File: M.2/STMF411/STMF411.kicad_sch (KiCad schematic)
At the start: 23 parts, among them M1 M.2_Key_E, Q1 2N7002, U1 LDK120PU-R_DFN6, U2 STM32F411CCUx, Y1 16 MHz

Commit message: touchups to f411
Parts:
- added L1: TapTap Logo, LogoSmall:tt_4mm, symbol Mechanical:MountingHole
- added SW1: RESET, LogoSmall:LogoSmall, symbol Switch:SW_SPST
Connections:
- net +3V3: now also SW1.2 (B)
- net BOOT0: now also SW1.1 (A)
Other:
- note added: "Fancy Logos and shit"
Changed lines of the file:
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@@
     (stroke (width 0) (type solid) (color 0 0 0 0))
   )
-  (polyline (pts (xy 17.145 80.01) (xy 17.145 101.6))
+  (polyline (pts (xy 17.145 81.28) (xy 17.145 102.87))
     (stroke (width 0) (type solid) (color 0 0 0 0))
   )
@@
     (stroke (width 0) (type solid) (color 141 210 114 1))
   )
+  (polyline (pts (xy 17.145 118.11) (xy 100.33 118.11))
+    (stroke (width 0) (type solid) (color 0 0 0 0))
+  )
   (wire (pts (xy 38.735 29.21) (xy 46.355 29.21))
     (stroke (width 0) (type solid) (color 141 210 114 1))
@@
     (stroke (width 0) (type default) (color 0 0 0 0))
   )
+  (polyline (pts (xy 283.845 13.335) (xy 283.845 127.635))
+    (stroke (width 0) (type default) (color 0 0 0 0))
+  )
+  (wire (pts (xy 144.145 31.115) (xy 146.685 31.115))
+    (stroke (width 0) (type default) (color 0 0 0 0))
+  )
+  (wire (pts (xy 19.685 38.1) (xy 19.685 34.29))
+    (stroke (width 0) (type solid) (color 141 210 114 1))
+  )
+  (polyline (pts (xy 17.145 19.05) (xy 56.515 19.05))
+    (stroke (width 0) (type solid) (color 0 0 0 0))
+  )
+  (wire (pts (xy 108.585 29.21) (xy 108.585 31.75))
+    (stroke (width 0) (type default) (color 0 0 0 0))
+  )
+  (wire (pts (xy 106.68 53.975) (xy 106.68 52.705))
+    (stroke (width 0) (type solid) (color 141 210 114 1))
+  )
+  (wire (pts (xy 106.68 46.355) (xy 126.365 46.355))
+    (stroke (width 0) (type default) (color 0 0 0 0))
+  )
+  (polyline (pts (xy 95.25 19.05) (xy 182.245 19.05))
+    (stroke (width 0) (type solid) (color 0 0 0 0))
+  )
+  (wire (pts (xy 144.145 109.855) (xy 146.685 109.855))
+    (stroke (width 0) (type default) (color 0 0 0 0))
+  )
+  (wire (pts (xy 218.44 32.385) (xy 233.045 32.385))
+    (stroke (width 0) (type default) (color 0 0 0 0))
+  )
+  (wire (pts (xy 126.365 53.975) (xy 119.38 53.975))
+    (stroke (width 0) (type default) (color 0 0 0 0))
+  )
+  (wire (pts (xy 46.99 62.23) (xy 46.99 64.77))
+    (stroke (width 0) (type default) (color 0 0 0 0))
+  )
+  (wire (pts (xy 48.895 29.21) (xy 46.355 29.21))
+    (stroke (width 0) (type solid) (color 141 210 114 1))
+  )
+  (wire (pts (xy 141.605 109.855) (xy 144.145 109.855))
+    (stroke (width 0) (type default) (color 0 0 0 0))
+  )
+  (wire (pts (xy 275.59 29.845) (xy 260.985 29.845))
+    (stroke (width 0) (type default) (color 0 0 0 0))
+  )
+  (polyline (pts (xy 17.145 76.835) (xy 92.075 76.835))
+    (stroke (width 0) (type solid) (color 0 0 0 0))
+  )
+  (wire (pts (xy 40.64 62.23) (xy 40.64 66.04))
+    (stroke (width 0) (type default) (color 0 0 0 0))
+  )
+  (wire (pts (xy 139.065 109.855) (xy 141.605 109.855))
+    (stroke (width 0) (type default) (color 0 0 0 0))
+  )
+  (polyline (pts (xy 56.515 19.05) (xy 56.515 48.26))
+    (stroke (width 0) (type solid) (color 0 0 0 0))
+  )
+  (wire (pts (xy 90.17 88.9) (xy 80.01 88.9))
+    (stroke (width 0) (type solid) (color 141 210 114 1))
+  )
   (wire (pts (xy 19.685 24.13) (xy 46.355 24.13))
-    (stroke (width 0) (type solid) (color 141 210 114 1))
-  )
-  (polyline (pts (xy 283.845 13.335) (xy 283.845 127.635))
-    (stroke (width 0) (type default) (color 0 0 0 0))
-  )
-  (wire (pts (xy 144.145 31.115) (xy 146.685 31.115))
-    (stroke (width 0) (type default) (color 0 0 0 0))
-  )
-  (wire (pts (xy 19.685 38.1) (xy 19.685 34.29))
-    (stroke (width 0) (type solid) (color 141 210 114 1))
-  )
-  (polyline (pts (xy 17.145 19.05) (xy 56.515 19.05))
-    (stroke (width 0) (type solid) (color 0 0 0 0))
-  )
-  (wire (pts (xy 108.585 29.21) (xy 108.585 31.75))
-    (stroke (width 0) (type default) (color 0 0 0 0))
-  )
-  (wire (pts (xy 106.68 53.975) (xy 106.68 52.705))
-    (stroke (width 0) (type solid) (color 141 210 114 1))
-  )
-  (wire (pts (xy 106.68 46.355) (xy 126.365 46.355))
-    (stroke (width 0) (type default) (color 0 0 0 0))
-  )
-  (polyline (pts (xy 95.25 19.05) (xy 182.245 19.05))
-    (stroke (width 0) (type solid) (color 0 0 0 0))
-  )
-  (wire (pts (xy 144.145 109.855) (xy 146.685 109.855))
-    (stroke (width 0) (type default) (color 0 0 0 0))
-  )
-  (wire (pts (xy 218.44 32.385) (xy 233.045 32.385))
-    (stroke (width 0) (type default) (color 0 0 0 0))
-  )
-  (wire (pts (xy 126.365 53.975) (xy 119.38 53.975))
-    (stroke (width 0) (type default) (color 0 0 0 0))
-  )
-  (wire (pts (xy 46.99 62.23) (xy 46.99 64.77))
-    (stroke (width 0) (type default) (color 0 0 0 0))
-  )
-  (wire (pts (xy 48.895 29.21) (xy 46.355 29.21))
-    (stroke (width 0) (type solid) (color 141 210 114 1))
-  )
-  (wire (pts (xy 141.605 109.855) (xy 144.145 109.855))
-    (stroke (width 0) (type default) (color 0 0 0 0))
-  )
-  (wire (pts (xy 275.59 29.845) (xy 260.985 29.845))
-    (stroke (width 0) (type default) (color 0 0 0 0))
-  )
-  (polyline (pts (xy 17.145 76.835) (xy 92.075 76.835))
-    (stroke (width 0) (type solid) (color 0 0 0 0))
-  )
-  (wire (pts (xy 40.64 62.23) (xy 40.64 66.04))
-    (stroke (width 0) (type default) (color 0 0 0 0))
-  )
-  (wire (pts (xy 139.065 109.855) (xy 141.605 109.855))
-    (stroke (width 0) (type default) (color 0 0 0 0))
-  )
-  (polyline (pts (xy 56.515 19.05) (xy 56.515 48.26))
-    (stroke (width 0) (type solid) (color 0 0 0 0))
-  )
-  (wire (pts (xy 90.17 88.9) (xy 80.01 88.9))
     (stroke (width 0) (type solid) (color 141 210 114 1))
   )
@@
     (stroke (width 0) (type default) (color 0 0 0 0))
   )
+  (polyline (pts (xy 100.33 118.11) (xy 100.33 106.68))
+    (stroke (width 0) (type solid) (color 0 0 0 0))
+  )
   (wire (pts (xy 46.355 43.18) (xy 38.735 43.18))
     (stroke (width 0) (type solid) (color 141 210 114 1))
@@
     (stroke (width 0) (type solid) (color 0 0 0 0))
   )
+  (polyline (pts (xy 17.145 106.68) (xy 17.145 118.11))
+    (stroke (width 0) (type solid) (color 0 0 0 0))
+  )
   (wire (pts (xy 31.115 93.98) (xy 42.545 93.98))
     (stroke (width 0) (type solid) (color 141 210 114 1))
@@
   (polyline (pts (xy 283.845 13.335) (xy 186.055 13.335))
     (stroke (width 0) (type default) (color 0 0 0 0))
+  )
+  (polyline (pts (xy 100.33 106.68) (xy 17.145 106.68))
+    (stroke (width 0) (type solid) (color 0 0 0 0))
   )
   (polyline (pts (xy 186.055 13.335) (xy 13.335 13.335))
@@
     (effects (font (size 1.27 1.27)) (justify left bottom))
   )
+  (text "Fancy Logos and shit" (at 17.145 105.41 0)
+    (effects (font (size 1.27 1.27)) (justify left bottom))
+  )
   (text "Microcontroller Decoupling" (at 17.145 80.01 0)
     (effects (font (size 1.27 1.27)) (justify left bottom))
@@
     (property "Intersheet References" "${INTERSHEET_REFS}" (id 0) (at 120.2024 71.6756 0)
       (effects (font (size 1.27 1.27)) (justify right) hide)
+    )
+  )
+  (global_label "reset" (shape input) (at 54.61 112.395 0) (fields_autoplaced)
+    (effects (font (size 1.27 1.27)) (justify left))
+    (property "Intersheet References" "${INTERSHEET_REFS}" (id 0) (at 61.7402 112.4744 0)
+      (effects (font (size 1.27 1.27)) (justify left) hide)
     )
   )
@@
     (pin "1")
   )
+  (symbol (lib_id "Switch:SW_SPST") (at 49.53 112.395 0) (mirror y) (unit 1)
+    (in_bom yes) (on_board yes)
+    (property "Reference" "SW1" (id 0) (at 38.735 110.49 0))
+    (property "Value" "RESET" (id 1) (at 38.735 113.03 0))
+    (property "Footprint" "LogoSmall:LogoSmall" (id 2) (at 49.53 112.395 0)
+      (effects (font (size 1.27 1.27)) hide)
+    )
+    (property "Datasheet" "~" (id 3) (at 49.53 112.395 0)
+      (effects (font (size 1.27 1.27)) hide)
+    )
+    (pin "1")
+    (pin "2")
+  )
   (symbol (lib_id "power:+5V") (at 275.59 29.845 0) (unit 1)
     (in_bom yes) (on_board yes)
@@
     (pin "1")
   )
+  (symbol (lib_id "power:+3.3V") (at 44.45 112.395 0) (unit 1)
+    (in_bom yes) (on_board yes)
+    (property "Reference" "#PWR?" (id 0) (at 44.45 116.205 0)
+      (effects (font (size 1.27 1.27)) hide)
+    )
+    (property "Value" "+3.3V" (id 1) (at 48.26 109.855 0))
+    (property "Footprint" "" (id 2) (at 44.45 112.395 0)
+      (effects (font (size 1.27 1.27)) hide)
+    )
+    (property "Datasheet" "" (id 3) (at 44.45 112.395 0)
+      (effects (font (size 1.27 1.27)) hide)
+    )
+    (pin "1")
+  )
   (symbol (lib_id "power:PWR_FLAG") (at 260.985 29.845 0) (unit 1)
     (in_bom yes) (on_board yes)
@@
     )
     (pin "1")
+  )
+  (symbol (lib_id "Mechanical:MountingHole") (at 71.755 111.76 0) (unit 1)
+    (in_bom yes) (on_board yes) (fields_autoplaced)
+    (property "Reference" "L1" (id 0) (at 74.93 110.4899 0)
+      (effects (font (size 1.27 1.27)) (justify left))
+    )
+    (property "Value" "TapTap Logo" (id 1) (at 74.93 113.0299 0)
+      (effects (font (size 1.27 1.27)) (justify left))
+    )
+    (property "Footprint" "LogoSmall:tt_4mm" (id 2) (at 71.755 111.76 0)
+      (effects (font (size 1.27 1.27)) hide)
+    )
+    (property "Datasheet" "~" (id 3) (at 71.755 111.76 0)
+      (effects (font (size 1.27 1.27)) hide)
+    )
   )
   (symbol (lib_id "power:GND") (at 106.68 53.975 0) (unit 1)
@@
       (reference "#PWR0122") (unit 1) (value "+3.3V") (footprint "")
     )
+    (path "/ad402068-7356-4a93-a5af-216a06e3804c"
+      (reference "#PWR?") (unit 1) (value "+3.3V") (footprint "")
+    )
     (path "/42ec88f7-d7f3-40cf-8759-f8c5477df41e"
       (reference "C1") (unit 1) (value "4.7uF") (footprint "Capacitor_SMD:C_0402_1005Metric")
@@
       (reference "H1") (unit 1) (value "MountingHole_Pad") (footprint "MountingHole:MountingHole_3.2mm_M3_Pad_Via")
     )
+    (path "/c6faf540-b2b4-4eb8-b3ae-c8820f05ccf2"
+      (reference "L1") (unit 1) (value "TapTap Logo") (footprint "LogoSmall:tt_4mm")
+    )
     (path "/09ab82c3-34e9-44f6-bcc6-a88b0ac9235b"
       (reference "M1") (unit 1) (value "M.2_Key_E") (footprint "m2ngff:m2-padKeyE")
@@
       (reference "R5") (unit 1) (value "100k") (footprint "Resistor_SMD:R_0402_1005Metric")
     )
+    (path "/7cf0f891-8a1a-40d2-a263-a0d273d44d57"
+      (reference "SW1") (unit 1) (value "RESET") (footprint "LogoSmall:LogoSmall")
+    )
     (path "/91a43a45-d59b-41ce-8612-b88cf8bbc380"

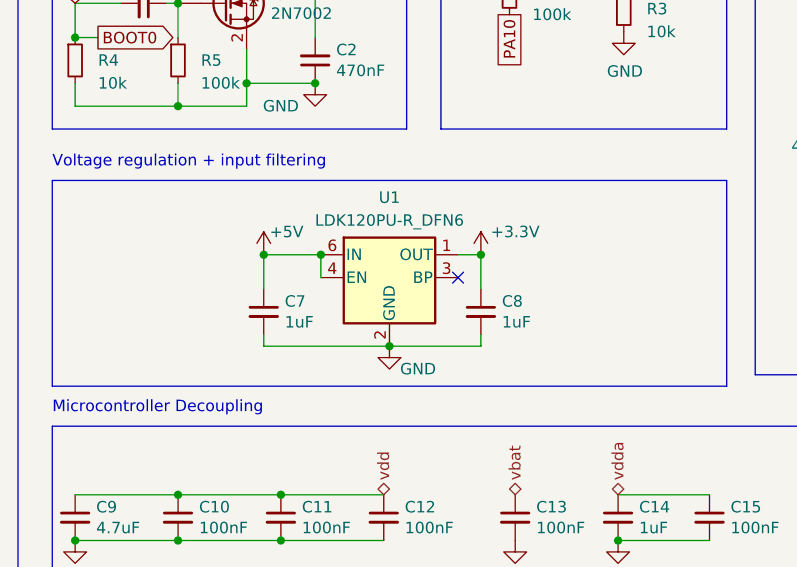
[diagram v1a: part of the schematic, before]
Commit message: finalize f411 for the last time. change to sot-23 ldo
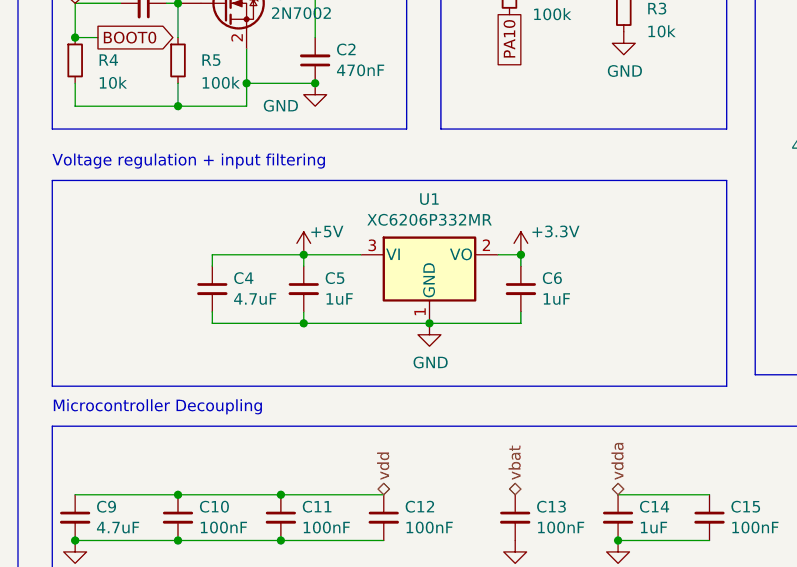
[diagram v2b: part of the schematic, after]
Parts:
- removed C7, C8: 1uF, Capacitor_SMD:C_0402_1005Metric, symbol Device:C_Small
- removed U1: LDK120PU-R_DFN6, Package_DFN_QFN:DFN-6_1.3x1.2mm_P0.4mm, symbol Regulator_Linear:LDK130PU33R_DFN6
- added C4: 4.7uF, Capacitor_SMD:C_0402_1005Metric, symbol Device:C_Small
- added C5, C6: 1uF, Capacitor_SMD:C_0402_1005Metric, symbol Device:C_Small
- added U1: XC6206P332MR, Package_TO_SOT_SMD:SOT-23, symbol Regulator_Linear:XC6206PxxxMR
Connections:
- net +3V3: now also C6.1, U1.2 (VO)
- net +5V: now also C4.1, C5.1, U1.3 (VI)
- net GND: now also C4.2, C5.2, C6.2, U1.1 (GND)
- no-connect marks 1 -> 0
